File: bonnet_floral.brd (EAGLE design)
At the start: 65 x 30 mm, 11 parts, among them IC1 RASPBERRY_PI_ZERO_W_(V1.3)-WO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

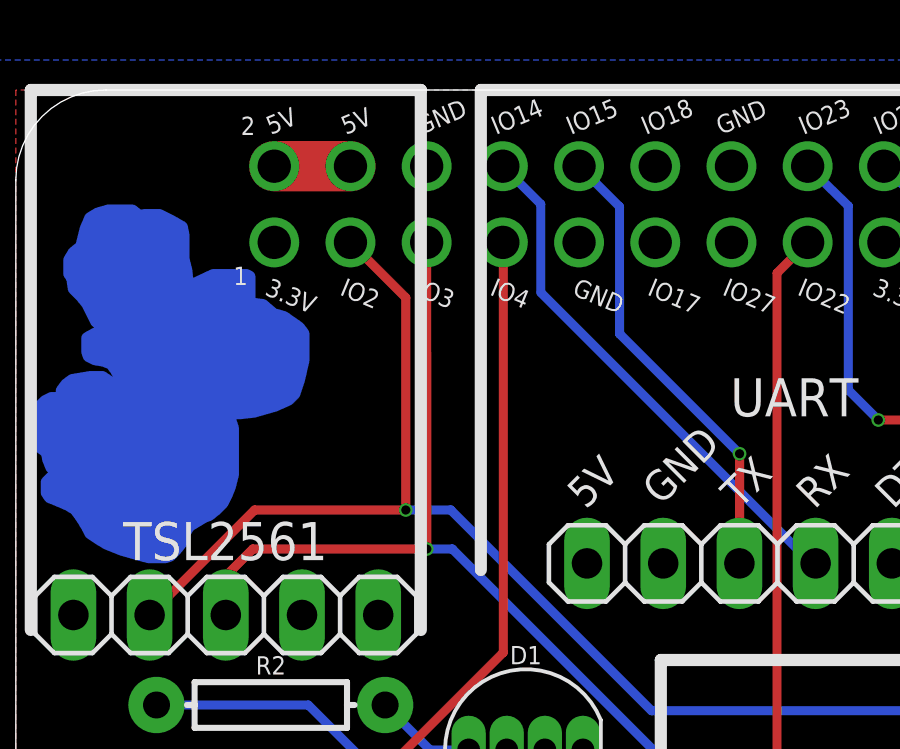
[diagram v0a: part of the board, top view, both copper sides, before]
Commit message: Add Serial Port 5V power feed
So in the original design the power coming from the serial port header
was intentionally left N/C, however there's argument that this might
have made some learning applications more complicated / expensive.
Attaching it to the main PI header 5V looks like it should work, and
feed into the same 5V linke the normal power header does.  Since the 5V
coming from the serial port chip seems to also feed directly from the
USB port this should be, at least, as safe as running power to it via
the main power header.

Signed-off-by: John 'Warthog9' Hawley <warthog9@eaglescrag.net>
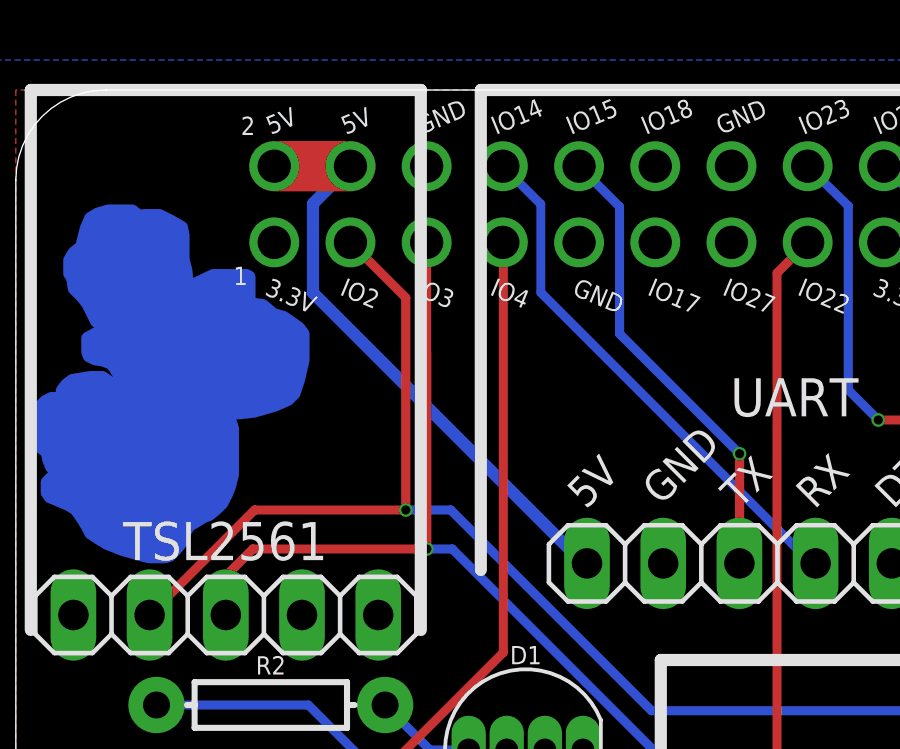
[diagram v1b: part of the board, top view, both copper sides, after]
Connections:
- removed net UART_5V: UART.6
- net 5V: now also UART.6
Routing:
- net 5V: track 2.54 -> 20.1 mm
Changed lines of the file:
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@@
 <contactref element="IC1" pad="2-5V"/>
 <wire x1="8.615" y1="27.46" x2="11.155" y2="27.46" width="1.6764" layer="1"/>
+<contactref element="UART" pad="6"/>
+<wire x1="11.155" y1="27.46" x2="9.906" y2="26.211" width="0.4064" layer="16"/>
+<wire x1="9.906" y1="26.211" x2="9.906" y2="23.241" width="0.4064" layer="16"/>
+<wire x1="9.906" y1="23.241" x2="18.927" y2="14.22" width="0.4064" layer="16"/>
+<wire x1="18.927" y1="14.22" x2="19.04" y2="14.22" width="0.4064" layer="16"/>
 </signal>
 <signal name="GND">
@@
 <wire x1="37.75" y1="22.37" x2="38.5" y2="21.62" width="0.3" layer="16"/>
 </signal>
-<signal name="UART_5V">
-<contactref element="UART" pad="6"/>
-</signal>
 <signal name="UART_3.3V">

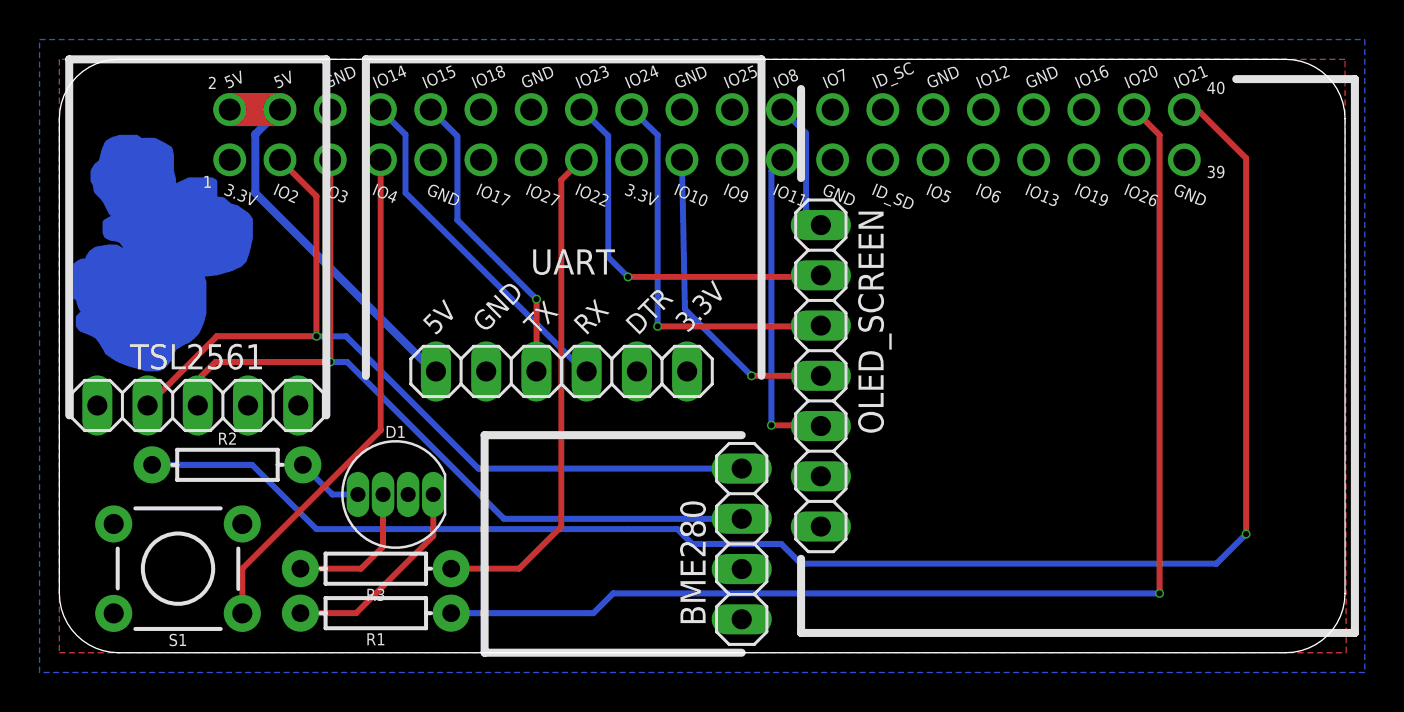
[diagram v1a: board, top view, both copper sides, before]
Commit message: Rotate oled screen 90deg counter-clockwise
This is basically a manufacturing optimization to move the under side
components of the oled screen away from the pi header.  There's a cap
that comes a bit close to the header and it's troublesome.  This shifts
the screen around and allows for just some kapton tape on the oled
screen to alleviate any possible touching / arcing.

Signed-off-by: John 'Warthog9' Hawley <warthog9@eaglescrag.net>
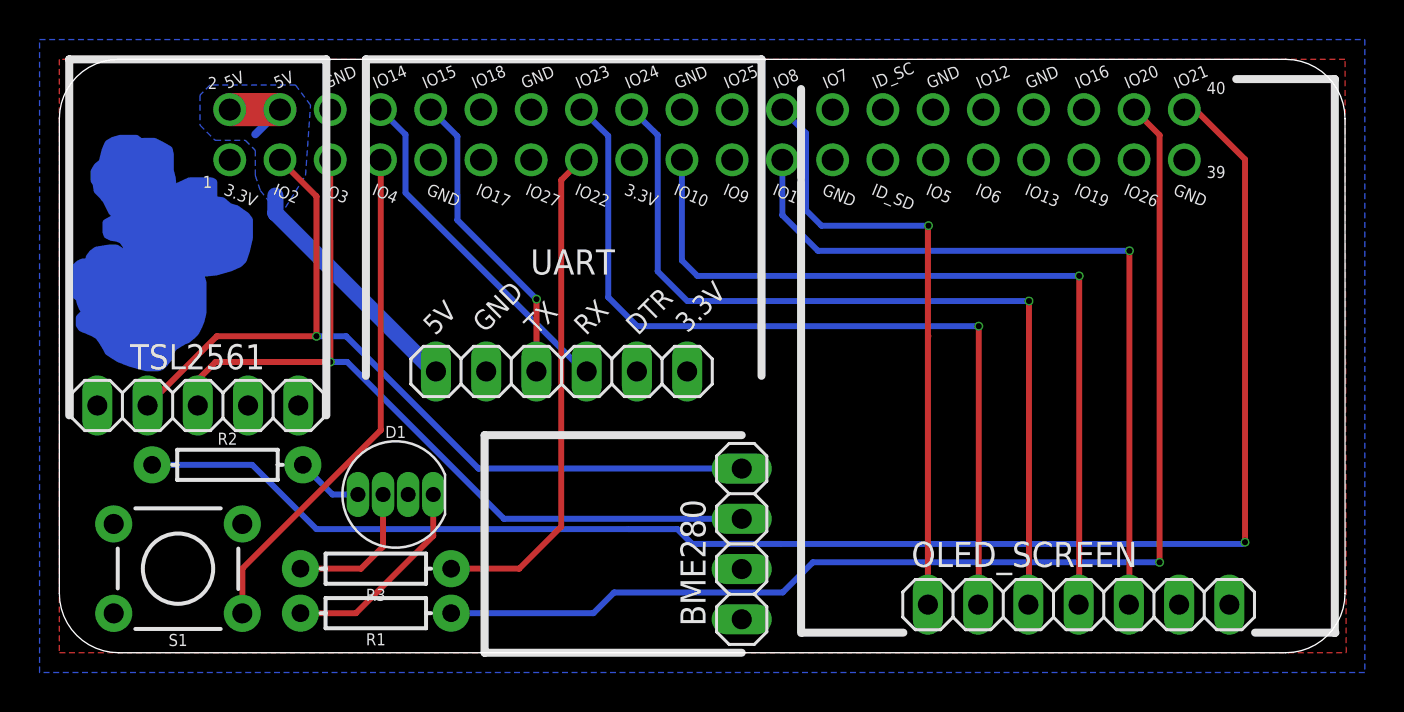
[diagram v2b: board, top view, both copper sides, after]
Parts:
- moved OLED_SCREEN 17.4 mm to (51.5, 2.43), turned to 180 degrees
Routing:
- net OLED_MOSI: track 15.8 -> 42.1 mm
- net OLED_CS: track 6.65 -> 31.3 mm, vias 0 -> 1
- net OLED_DC: track 19.2 -> 43.5 mm
- net OLED_RES: track 19.8 -> 43.5 mm
- net OLED_CLK: track 16.2 -> 39.0 mm
- net 5V: track 20.1 -> 16.6 mm
- net RGB_R: track 61.2 -> 60.3 mm
- net RGB_B: track 81.1 -> 80.4 mm
- added copper zone on layer 16, net 5V
